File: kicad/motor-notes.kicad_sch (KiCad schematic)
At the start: 0 parts

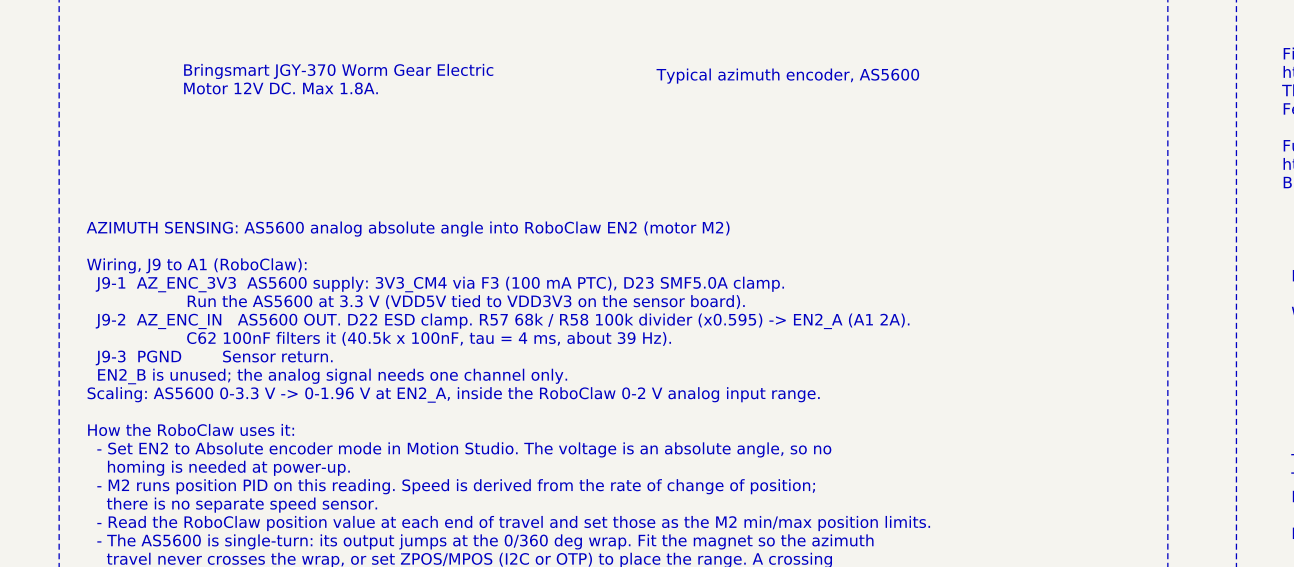
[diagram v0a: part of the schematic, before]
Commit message: Updates after latest Tomachie review
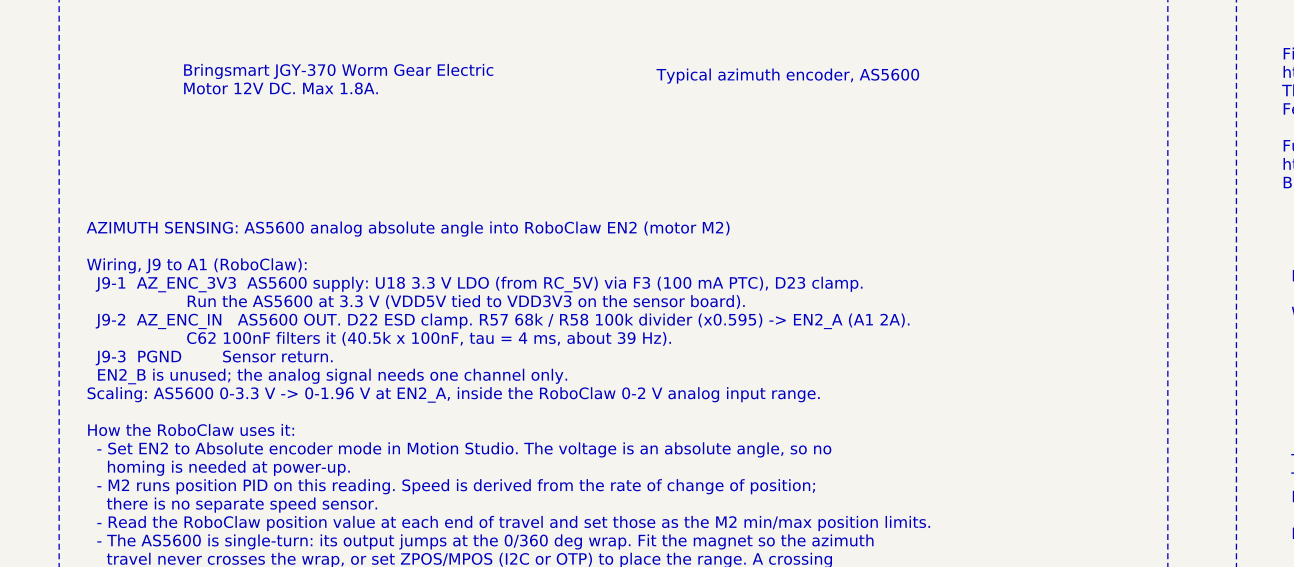
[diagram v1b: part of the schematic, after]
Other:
- note added: "AZIMUTH SENSING: AS5600 analog absolute angle into RoboClaw EN2 (motor M2) Wiring, J9 to A1 (RoboClaw): J9-1 AZ_ENC_3V3 AS5600 supply: U18 3.3 V LDO (from RC_5V) via F3 (100 mA PTC), D23 clamp. Run the AS5600 at 3.3 V (VDD5V tied to VDD3V3 on the sensor board). J9-2 AZ_ENC_IN AS5600 OUT. D22 ESD clamp. R57 68k / R58 100k divider (x0.595) -> EN2_A (A1 2A). C62 100nF filters it (40.5k x 100nF, tau 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"
- note removed: "AZIMUTH SENSING: AS5600 analog absolute angle into RoboClaw EN2 (motor M2) Wiring, J9 to A1 (RoboClaw): J9-1 AZ_ENC_3V3 AS5600 supply: 3V3_CM4 via F3 (100 mA PTC), D23 SMF5.0A clamp. Run the AS5600 at 3.3 V (VDD5V tied to VDD3V3 on the sensor board). J9-2 AZ_ENC_IN AS5600 OUT. D22 ESD clamp. R57 68k / R58 100k divider (x0.595) -> EN2_A (A1 2A). C62 100nF filters it (40.5k x 100nF, tau = 4 ms, abo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"
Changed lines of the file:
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@@
 		)
 	)
-	(text "AZIMUTH SENSING: AS5600 analog absolute angle into RoboClaw EN2 (motor M2)\n\nWiring, J9 to A1 (RoboClaw):\n  J9-1  AZ_ENC_3V3  AS5600 supply: 3V3_CM4 via F3 (100 mA PTC), D23 SMF5.0A clamp.\n                    Run the AS5600 at 3.3 V (VDD5V tied to VDD3V3 on the sensor board).\n  J9-2  AZ_ENC_IN   AS5600 OUT. D22 ESD clamp. R57 68k / R58 100k divider (x0.595) -> EN2_A (A1 2A).\n                    C62 100nF filters it (40.5k x 100nF, tau = 4 ms, about 39 Hz).\n  J9-3  PGND        Sensor return.\n  EN2_B is unused; the analog signal needs one channel only.\nScaling: AS5600 0-3.3 V -> 0-1.96 V at EN2_A, inside the RoboClaw 0-2 V analog input range.\n\nHow the RoboClaw uses it:\n  - Set EN2 to Absolute encoder mode in Motion Studio. The voltage is an absolute angle, so no\n    homing is needed at power-up.\n  - M2 runs position PID on this reading. Speed is derived from the rate of change of position;\n    there is no separate speed sensor.\n  - Read the RoboClaw position value at each end of travel and set those as the M2 min/max position limits.\n  - The AS5600 is single-turn: its output jumps at the 0/360 deg wrap. Fit the magnet so the azimuth\n    travel never crosses the wrap, or set ZPOS/MPOS (I2C or OTP) to place the range. A crossing\n    makes the position loop run away.\n  - The magnet must be on a shaft that turns at most one revolution over the full azimuth travel.\n\nAS5600 output loading (datasheet): full-range analog (the default) needs >= 100k. R57 + R58 = 168k, OK.\n  - OUT capacitive load 1 nF max: R57 isolates C62; keep the J9 cable short (about 100 pF/m).\n  - Divider source impedance is about 40k. If the RoboClaw EN2 pull-up stays on in Absolute mode it lifts\n    the reading: bench-check EN2_A with and without the RoboClaw; calibrate travel limits on hardware.\n  - J9 is powered from 3V3_CM4 (logic GND) but returns on PGND, so the sensor current crosses NT1."
+	(text "AZIMUTH SENSING: AS5600 analog absolute angle into RoboClaw EN2 (motor M2)\n\nWiring, J9 to A1 (RoboClaw):\n  J9-1  AZ_ENC_3V3  AS5600 supply: U18 3.3 V LDO (from RC_5V) via F3 (100 mA PTC), D23 clamp.\n                    Run the AS5600 at 3.3 V (VDD5V tied to VDD3V3 on the sensor board).\n  J9-2  AZ_ENC_IN   AS5600 OUT. D22 ESD clamp. R57 68k / R58 100k divider (x0.595) -> EN2_A (A1 2A).\n                    C62 100nF filters it (40.5k x 100nF, tau = 4 ms, about 39 Hz).\n  J9-3  PGND        Sensor return.\n  EN2_B is unused; the analog signal needs one channel only.\nScaling: AS5600 0-3.3 V -> 0-1.96 V at EN2_A, inside the RoboClaw 0-2 V analog input range.\n\nHow the RoboClaw uses it:\n  - Set EN2 to Absolute encoder mode in Motion Studio. The voltage is an absolute angle, so no\n    homing is needed at power-up.\n  - M2 runs position PID on this reading. Speed is derived from the rate of change of position;\n    there is no separate speed sensor.\n  - Read the RoboClaw position value at each end of travel and set those as the M2 min/max position limits.\n  - The AS5600 is single-turn: its output jumps at the 0/360 deg wrap. Fit the magnet so the azimuth\n    travel never crosses the wrap, or set ZPOS/MPOS (I2C or OTP) to place the range. A crossing\n    makes the position loop run away.\n  - The magnet must be on a shaft that turns at most one revolution over the full azimuth travel.\n\nAS5600 output loading (datasheet): full-range analog (the default) needs >= 100k. R57 + R58 = 168k, OK.\n  - OUT capacitive load 1 nF max: R57 isolates C62; keep the J9 cable short (about 100 pF/m).\n  - Divider source impedance is about 40k. If the RoboClaw EN2 pull-up stays on in Absolute mode it lifts\n    the reading: bench-check EN2_A with and without the RoboClaw; calibrate travel limits on hardware.\n  - J9 is powered from 3V3_CM4 (logic GND) but returns on PGND, so the sensor current crosses NT1."
 		(exclude_from_sim no)
 		(at 24.638 101.6 0)
